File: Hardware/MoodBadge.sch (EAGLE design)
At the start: 41 parts, among them U1 MCP73831

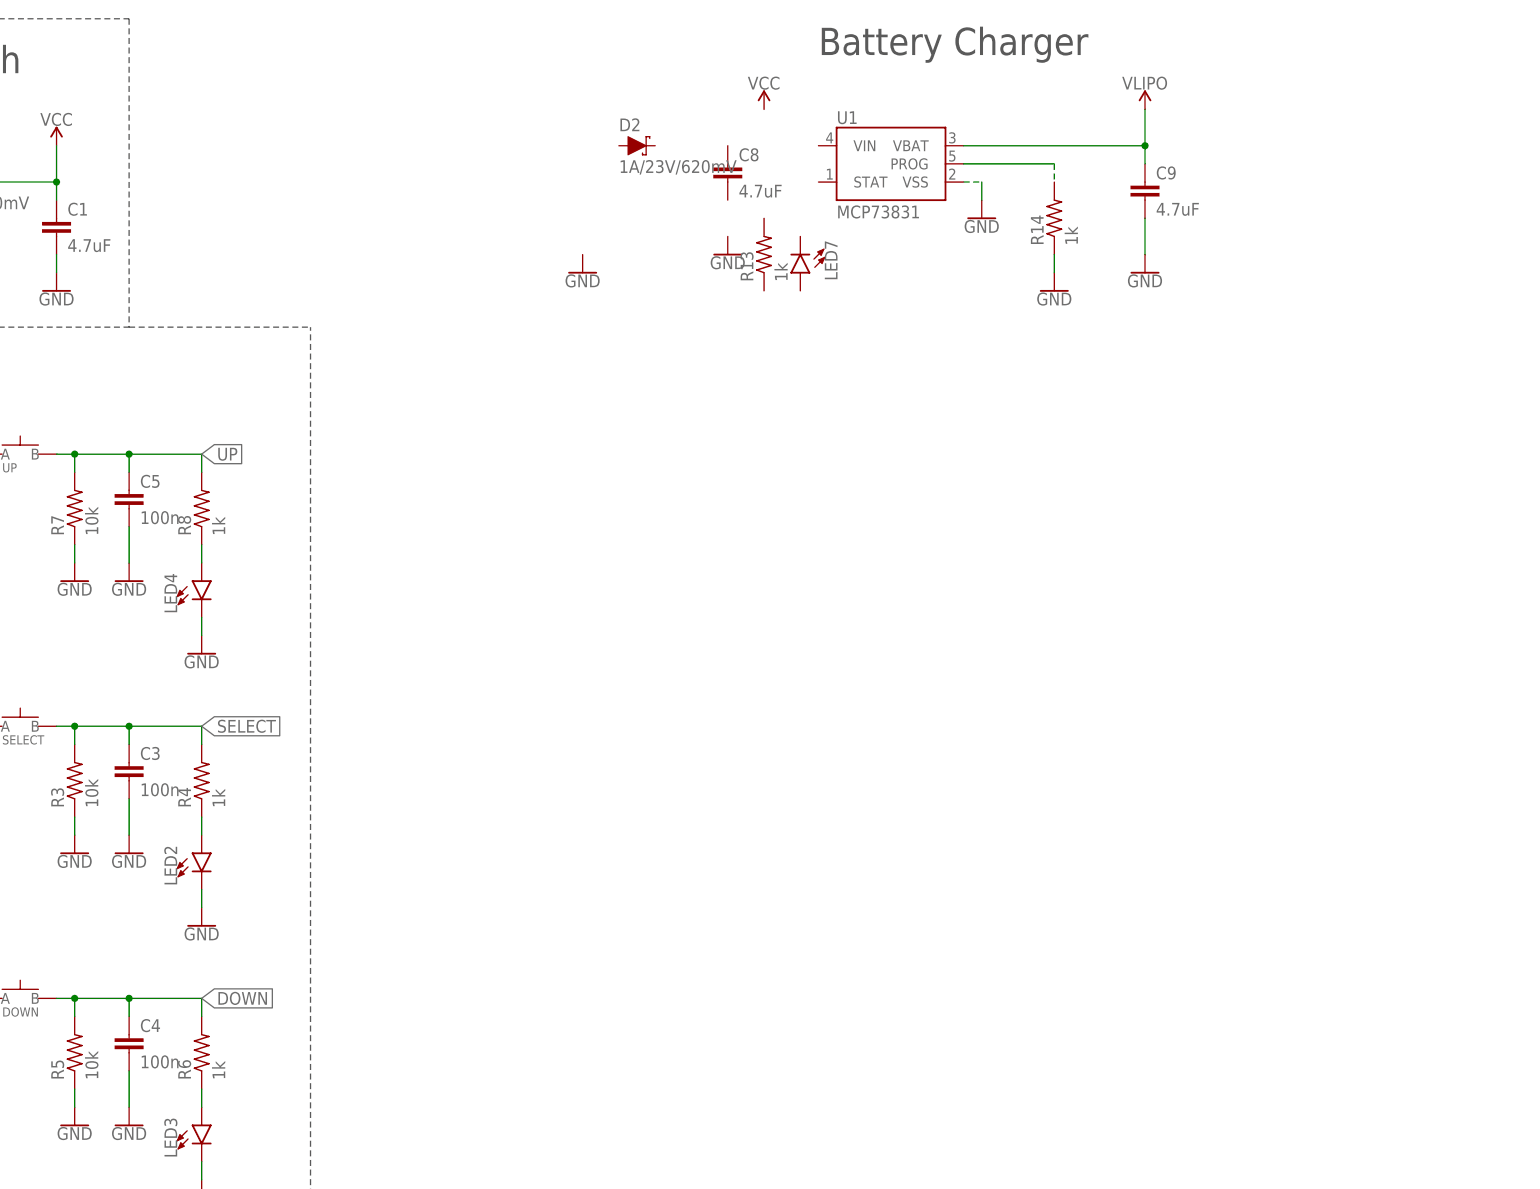
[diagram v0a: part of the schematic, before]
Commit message: Added battery charger and microcontroller sections
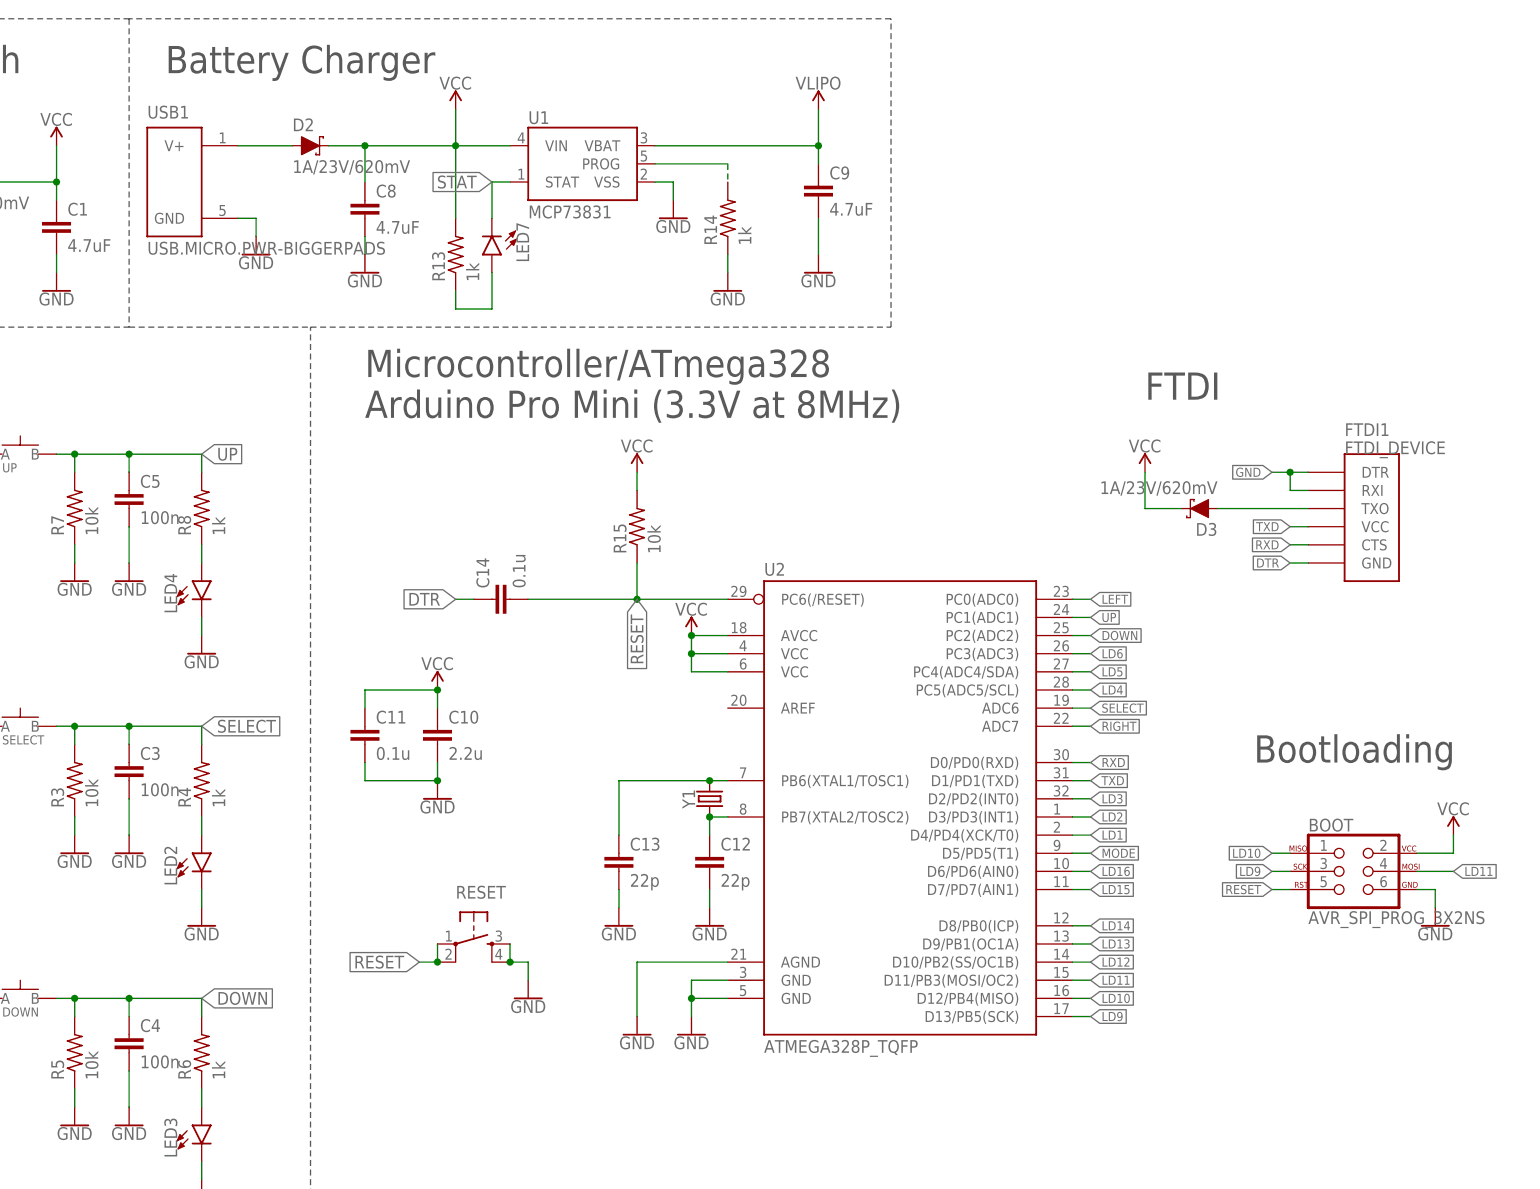
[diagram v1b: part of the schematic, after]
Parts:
- added BOOT: AVR_SPI_PROG_3X2NS, LinnesLab-Connectors:AVR_SPI_PROG_3X2NS
- added C10: 2.2u, LinnesLab-Passives:CAPACITOR0603
- added C11, C14: 0.1u, LinnesLab-Passives:CAPACITOR0603
- added C12, C13: 22p, LinnesLab-Passives:CAPACITOR0603
- added D3: 1A/23V/620mV, LinnesLab-DiscreteSemi:SCHOTTKY-USC
- added FTDI1: FTDI_DEVICE, LinnesLab-Connectors:FTDI_DEVICE
- added R15: 10k, LinnesLab-Passives:RESISTOR0603
- added RESET: (no value), LinnesLab-Switches:SPST-PTS830GG140
- added U2: ATMEGA328P_TQFP, LinnesLab-Microcontrollers:ATMEGA328P_TQFP
- added USB1: USB.MICRO.PWR-BIGGERPADS, LinnesLab-Connectors:USB.MICRO.PWR-BIGGERPADS
- added Y1: (no value), LinnesLab-Clocks:CRYSTAL-CA-310
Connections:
- new net DTR: C14.1, FTDI1.GND
- new net LD1: U2.D4/PD4(XCK/T0)
- new net LD10: BOOT.1, U2.D12/PB4(MISO)
- new net LD11: BOOT.4, U2.D11/PB3(MOSI/OC2)
- new net LD12: U2.D10/PB2(SS/OC1B)
- new net LD13: U2.D9/PB1(OC1A)
- new net LD14: U2.D8/PB0(ICP)
- new net LD15: U2.D7/PD7(AIN1)
- new net LD16: U2.D6/PD6(AIN0)
- new net LD2: U2.D3/PD3(INT1)
- new net LD3: U2.D2/PD2(INT0)
- new net LD4: U2.PC5(ADC5/SCL)
- new net LD5: U2.PC4(ADC4/SDA)
- new net LD6: U2.PC3(ADC3)
- new net LD9: BOOT.3, U2.D13/PB5(SCK)
- new net N$1: D2.A, USB1.V+
- new net N$10: C12.1, U2.PB7(XTAL2/TOSC2), Y1.1
- new net N$12: D3.A, FTDI1.TXO
- new net N$6: LED7.A, R13.1
- new net N$8: C13.1, U2.PB6(XTAL1/TOSC1), Y1.2
- new net RESET: BOOT.5, C14.2, R15.1, RESET.1, RESET.2, U2.PC6(/RESET)
- new net RXD: FTDI1.CTS, U2.D0/PD0(RXD)
- new net STAT: LED7.C, U1.STAT
- new net TXD: FTDI1.VCC, U2.D1/PD1(TXD)
- net DOWN: now also U2.PC2(ADC2)
- net GND: now also BOOT.6, C10.2, C11.2, C12.2, C13.2, C8.2, FTDI1.DTR, FTDI1.RXI, RESET.3, RESET.4, U2.AGND, U2.GND@3, U2.GND@5, USB1.GND
- net LEFT: now also U2.PC0(ADC0)
- net MODE: now also U2.D5/PD5(T1)
- net RIGHT: now also U2.ADC7
- net SELECT: now also U2.ADC6
- net UP: now also U2.PC1(ADC1)
- net VCC: now also BOOT.2, C10.1, C11.1, C8.1, D2.C, D3.C, R13.2, R15.2, U1.VIN, U2.AVCC, U2.VCC@4, U2.VCC@6
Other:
- note added: "Bootloading"
- note added: "FTDI"
- note added: "Microcontroller/ATmega328 Arduino Pro Mini (3.3V at 8MHz)"
- moved on the sheet: C8, C9, D2, LED7, R13, R14, U1

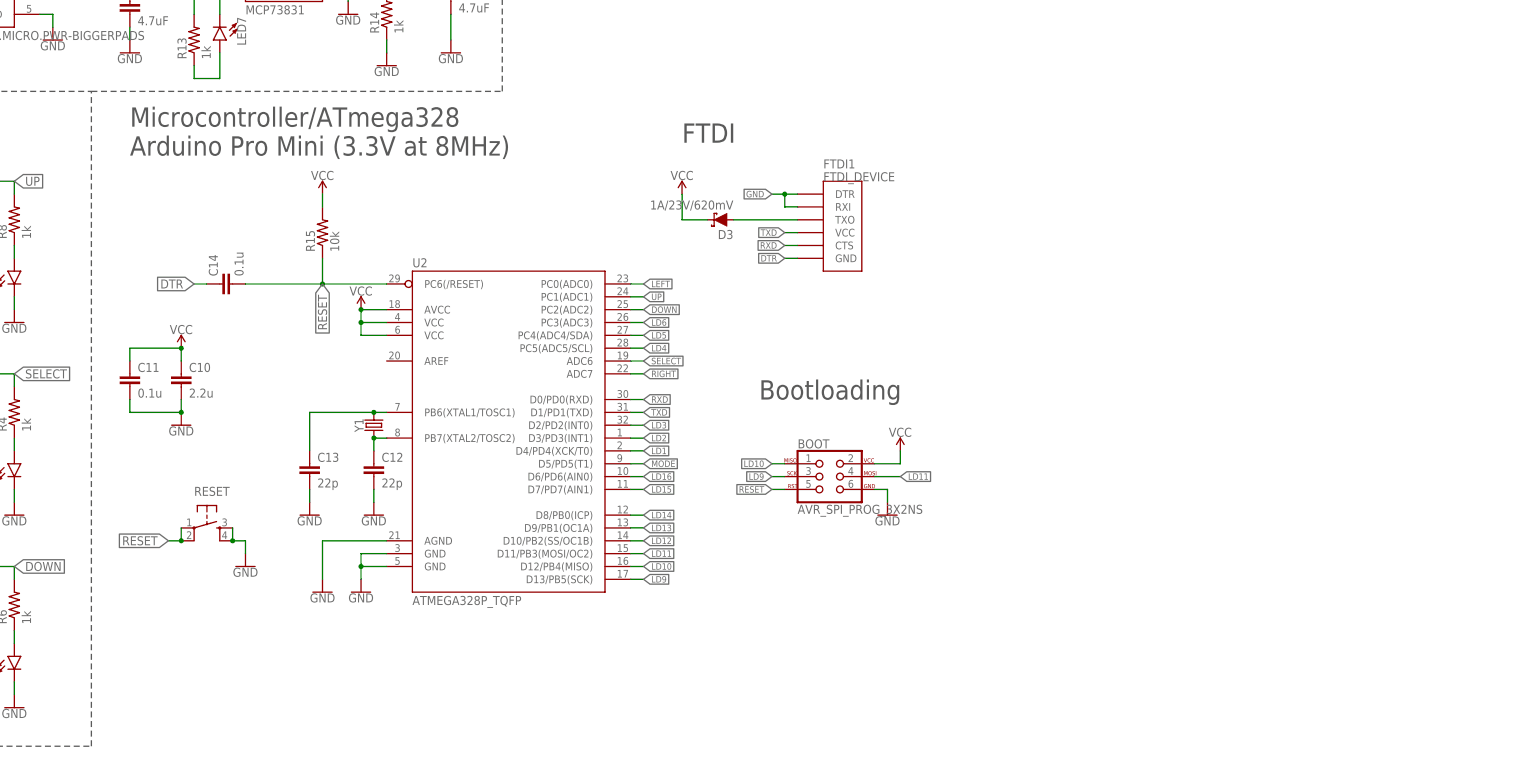
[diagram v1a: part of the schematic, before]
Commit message: Added LED matrix and fixed Arduino output pins
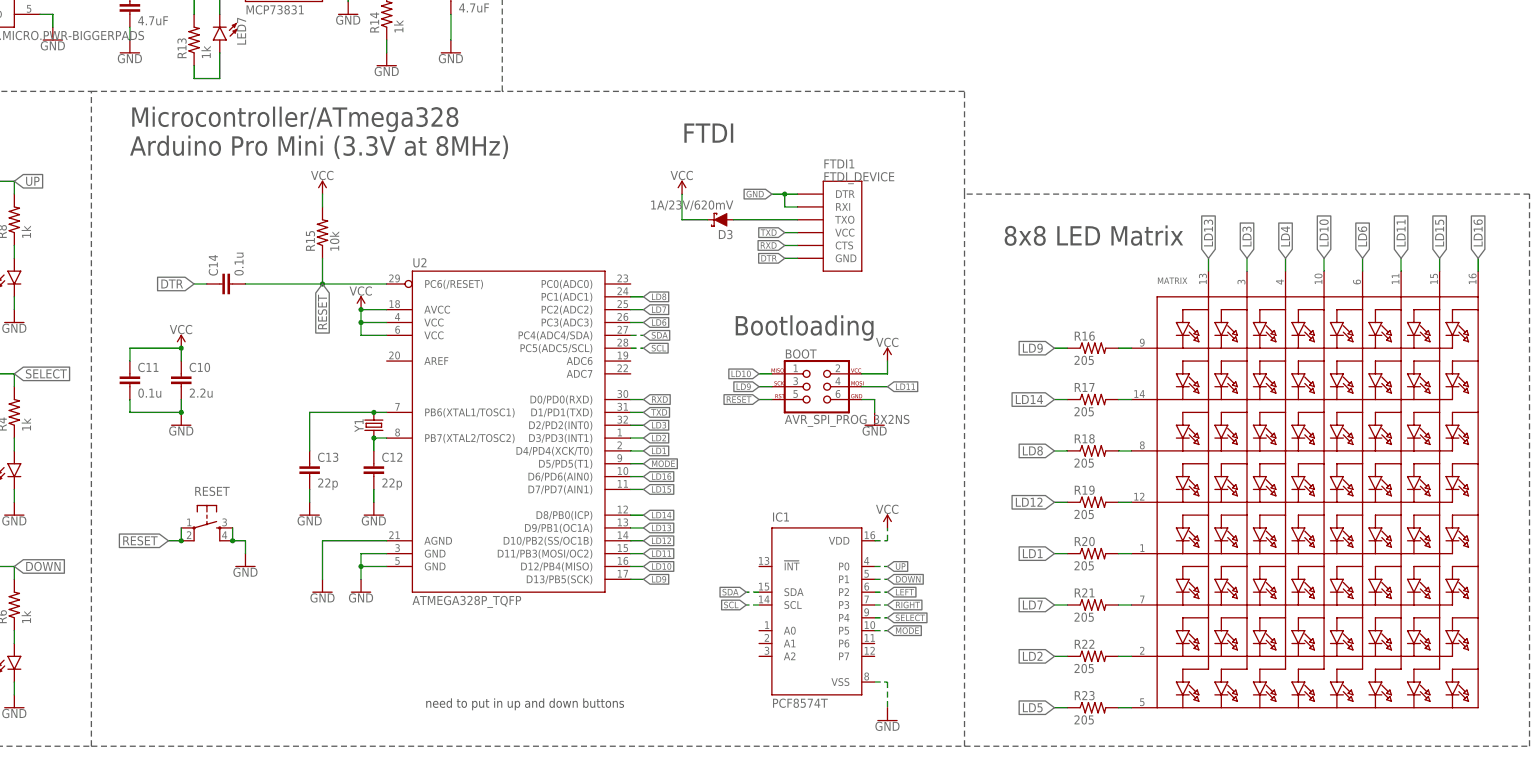
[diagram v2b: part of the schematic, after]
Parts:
- added IC1: PCF8574T, micro-philips:PCF8574T
- added MATRIX: (no value), adafruit:SEGMENT_8X8_ROWCATHODEBL-M12A883
- added R16, R17, R18, R19, R20, R21, R22, R23: 205, LinnesLab-Passives:RESISTOR0603
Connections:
- new net LD7: R21.1, U2.PC2(ADC2)
- new net LD8: R18.1, U2.PC1(ADC1)
- new net N$14: MATRIX.K1, R16.2
- new net N$15: MATRIX.K2, R17.2
- new net N$16: MATRIX.K3, R18.2
- new net N$17: MATRIX.K4, R19.2
- new net N$18: MATRIX.K5, R20.2
- new net N$19: MATRIX.K6, R21.2
- new net N$20: MATRIX.K7, R22.2
- new net N$21: MATRIX.K8, R23.2
- new net SCL: IC1.SCL, U2.PC5(ADC5/SCL)
- new net SDA: IC1.SDA, U2.PC4(ADC4/SDA)
- net DOWN: now also IC1.P1; no longer U2.PC2(ADC2)
- net GND: now also IC1.VSS
- net LD1: now also R20.1
- net LD10: now also MATRIX.A4
- net LD11: now also MATRIX.A6
- net LD12: now also R19.1
- net LD13: now also MATRIX.A1
- net LD14: now also R17.1
- net LD15: now also MATRIX.A7
- net LD16: now also MATRIX.A8
- net LD2: now also R22.1
- net LD3: now also MATRIX.A2
- net LD4: now also MATRIX.A3; no longer U2.PC5(ADC5/SCL)
- net LD5: now also R23.1; no longer U2.PC4(ADC4/SDA)
- net LD6: now also MATRIX.A5
- net LD9: now also R16.1
- net LEFT: now also IC1.P2; no longer U2.PC0(ADC0)
- net MODE: now also IC1.P5
- net RIGHT: now also IC1.P3; no longer U2.ADC7
- net SELECT: now also IC1.P4; no longer U2.ADC6
- net UP: now also IC1.P0; no longer U2.PC1(ADC1)
- net VCC: now also IC1.VDD
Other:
- note added: "8x8 LED Matrix"
- note added: "need to put in up and down buttons"
- moved on the sheet: BOOT

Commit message: Added remaining parts of circuit and port expander. Connected Pulse pin
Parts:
- added C15, C21: 100n, SparkFun-Capacitors:4.7UF-0603-6.3V-(10%)
- added C16, C17, C18: 4.7u, SparkFun-Capacitors:4.7UF-0603-6.3V-(10%)
- added C19: 2.2u, SparkFun-Capacitors:4.7UF-0603-6.3V-(10%)
- added C20: 1u, SparkFun-Capacitors:4.7UF-0603-6.3V-(10%)
- added LED8: (no value), LinnesLab-LED:LED0603
- added OP: OP-SINGLEOT, LinnesLab-AnalogIC:OP-SINGLEOT
- added PD: ADPS9008, LinnesLab-Sensors:ADPS9008
- added R24: 487, LinnesLab-Passives:RESISTOR0603
- added R25: 12k, LinnesLab-Passives:RESISTOR0603
- added R26: 10k, LinnesLab-Passives:RESISTOR0603
- added R27: 3.3M, LinnesLab-Passives:RESISTOR0603
- added R28, R29: 210k, LinnesLab-Passives:RESISTOR0603
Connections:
- new net N$22: LED8.C, R24.2
- new net N$23: C17.1, PD.OUT, R25.2
- new net N$24: C16.1, C17.2, C18.1
- new net N$25: C19.2, OPG$1.+IN, R28.1, R29.2
- new net N$26: C18.2, C19.1, R26.1
- new net N$28: OPG$1.-IN, R26.2, R27.1
- new net PULSE: OPG$1.OUT, R27.2, U2.D6/PD6(AIN0)
- net GND: now also C15.2, C16.2, C20.1, C21.2, OPG$2.V-, PD.GND, R24.1, R25.1, R29.1
- net LD16: now also U2.D5/PD5(T1); no longer U2.D6/PD6(AIN0)
- net MODE: no longer U2.D5/PD5(T1)
- net VCC: now also C15.1, C20.2, C21.1, LED8.A, OPG$2.V+, PD.VCC, R28.2
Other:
- note added: "Active Band-pass Filter"
- note added: "Trandsucer and Transimpedance Amp"
- note removed: "need to put in up and down buttons"

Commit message: Fixed incorrect values and made organizational adjustments
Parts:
- LED1: value (none) -> LEFT
- LED2: value (none) -> SELECT
- LED3: value (none) -> DOWN
- LED4: value (none) -> UP
- LED5: value (none) -> RIGHT
- LED6: value (none) -> MODE
- LED7: value (none) -> STAT
- R14: value 1k -> 10K
- Y1: value (none) -> Crystal-CA-310
- renumbered U1 to CHRG
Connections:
- net LD4: now also U2.ADC7
- net LD5: now also U2.ADC6
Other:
- note added: "Port Expander"
